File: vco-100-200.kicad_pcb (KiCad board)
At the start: 4 copper layers, 55 x 30 mm, 88 parts, among them J3 Conn_01x06_Pin, Q1 BC847C, Q10 BC847C, Q6 MMBFJ310, Q7 BC847C, Q8 MMBFJ310, Q9 BFR92P, U1 ADF4116, U2 MCP1804x-3302xOT, U3 MCP1804x-5002xOT

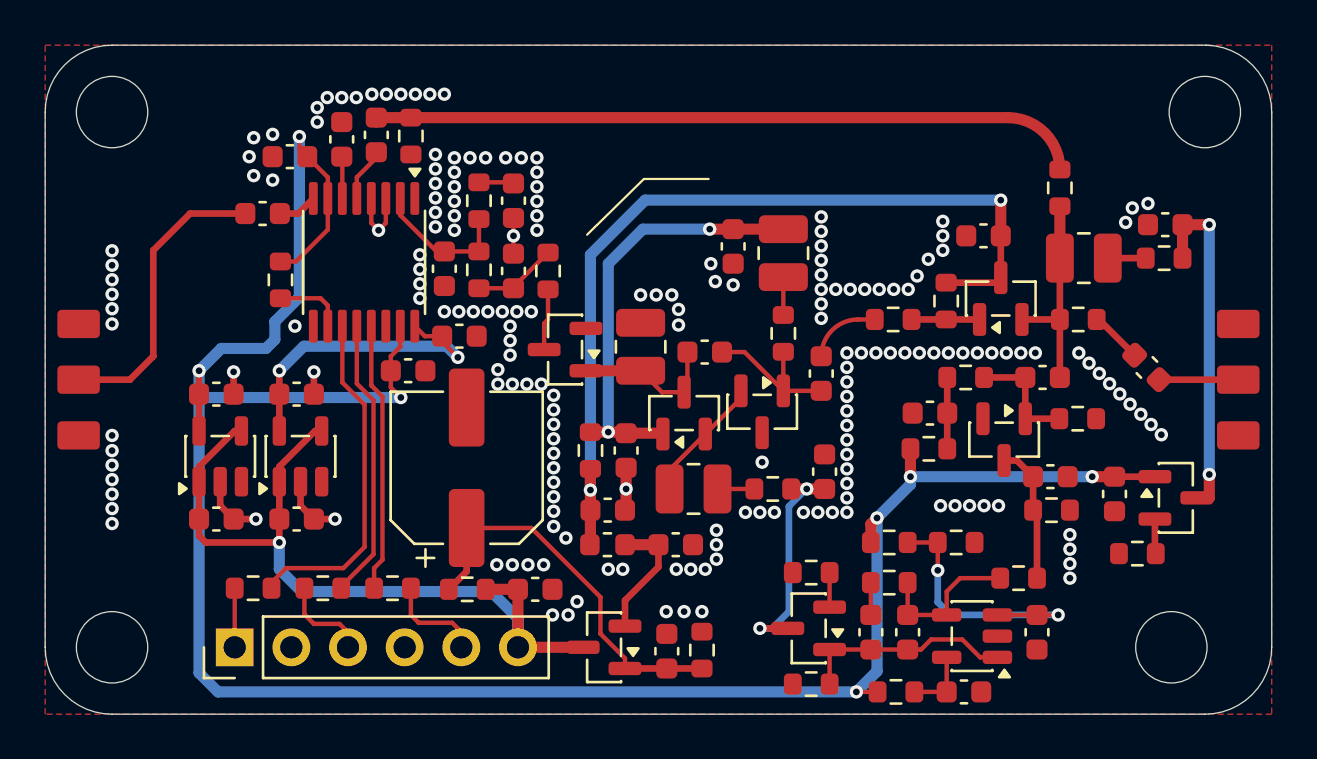
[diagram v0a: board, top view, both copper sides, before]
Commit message: Update pcb routing, add 50 Ohm net classes
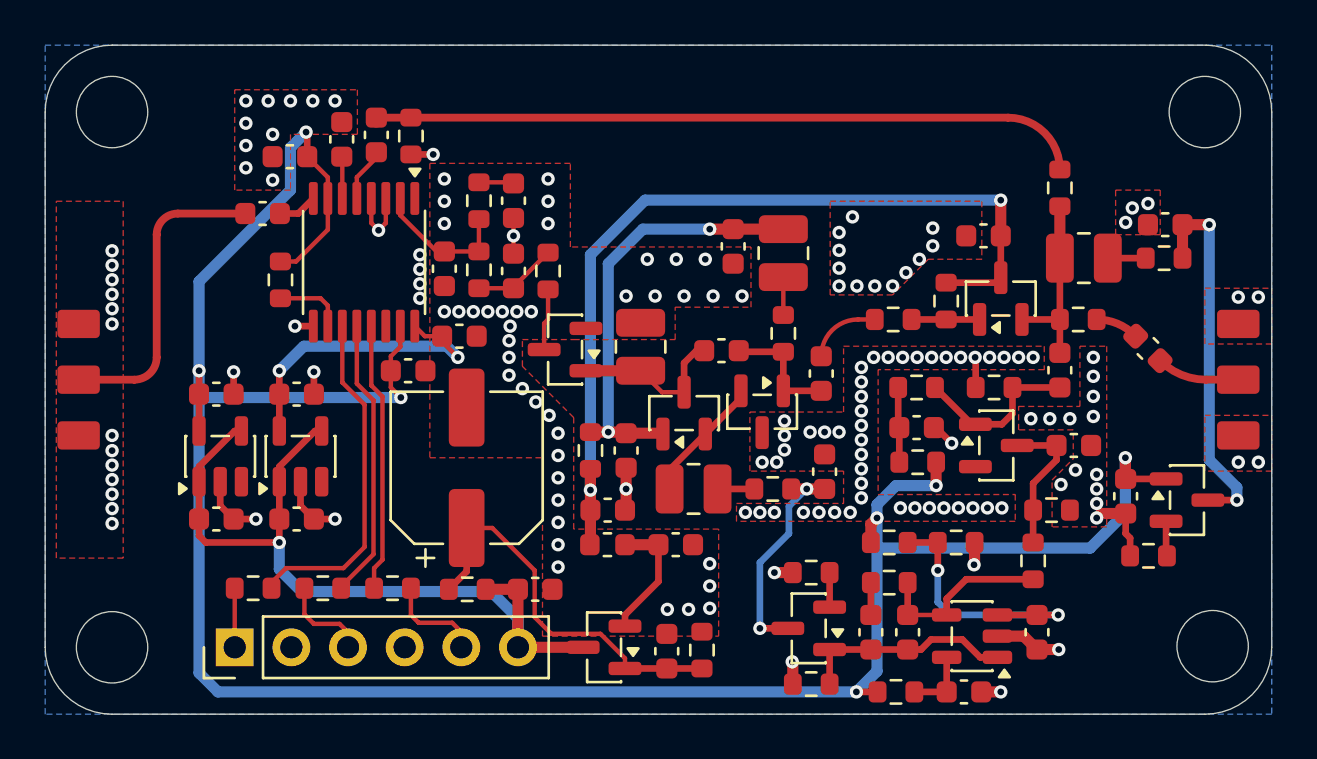
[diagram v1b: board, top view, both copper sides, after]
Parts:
- moved R23 4.00 mm to (162.6, 123.8), turned to 180 degrees
- moved R9 2.25 mm to (159.1, 123.8)
- moved H4 1.85 mm to (172.4, 135.4)
- moved C21 1.75 mm to (166.2, 126.5)
- moved R29 1.01 mm to (164.3, 131.6), turned to -90 degrees
- moved C19 0.88 mm to (159.1, 125.7), turned to 0 degrees
- moved C34 0.86 mm to (169.5, 122.1)
- moved C18 0.84 mm to (165.6, 123.1), turned to -90 degrees
- moved R25 0.78 mm to (159.2, 127.2), turned to 180 degrees
- moved C24 0.75 mm to (150.4, 122.2)
- moved C31 0.51 mm to (168.5, 128.7)
- moved Q10 0.51 mm to (171.2, 128.9)
- moved R41 0.51 mm to (169.5, 131.4)
- moved D4 0.44 mm to (162.7, 126.5), turned to 0 degrees
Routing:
- net Earth: track 14.4 -> 28.8 mm, vias 187 -> 159
- net /PLL/Vdd: track 104.7 -> 110.9 mm
- net Net-(D4-A): track 5.22 -> 7.71 mm
- net Net-(Q8-D): track 6.92 -> 5.47 mm
- net Net-(Q10-C): track 15.5 -> 16.9 mm
- net Net-(DA2--): track 6.90 -> 8.16 mm
- net Net-(Q9-E): track 9.38 -> 8.28 mm
- net Net-(D5-A1): track 6.66 -> 7.45 mm
- net /PLL/REFin: track 13.3 -> 14.0 mm
- added copper zone on B.Cu, net Earth
